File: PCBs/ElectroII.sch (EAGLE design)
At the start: 11 parts

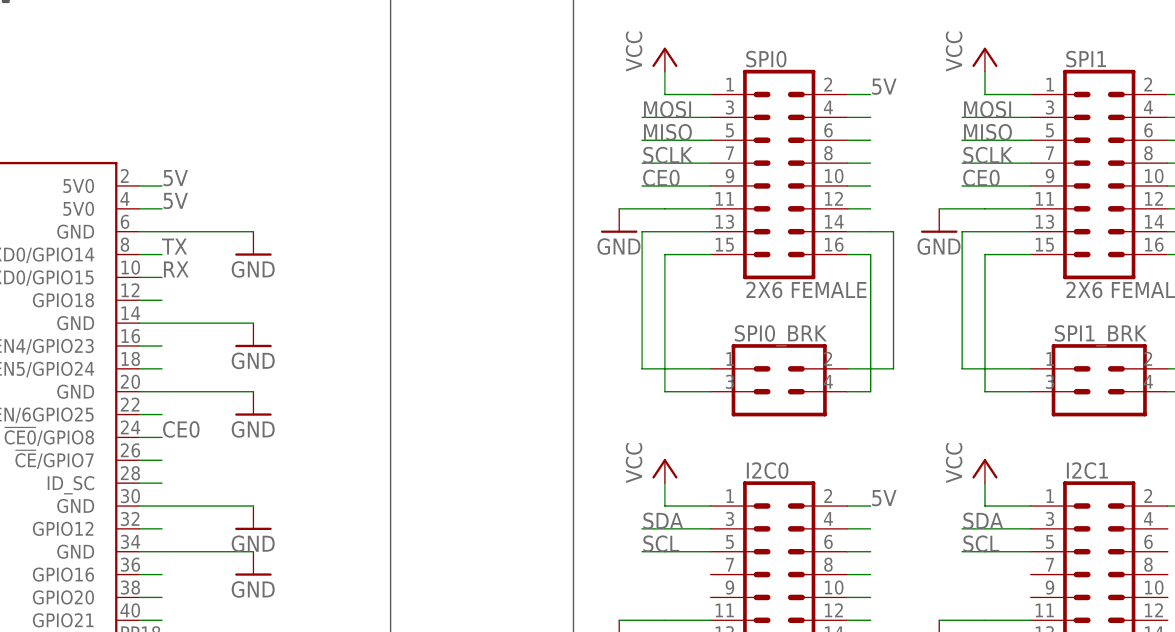
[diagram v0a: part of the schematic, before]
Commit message: Fixed a few mistakes in sensor breakouts
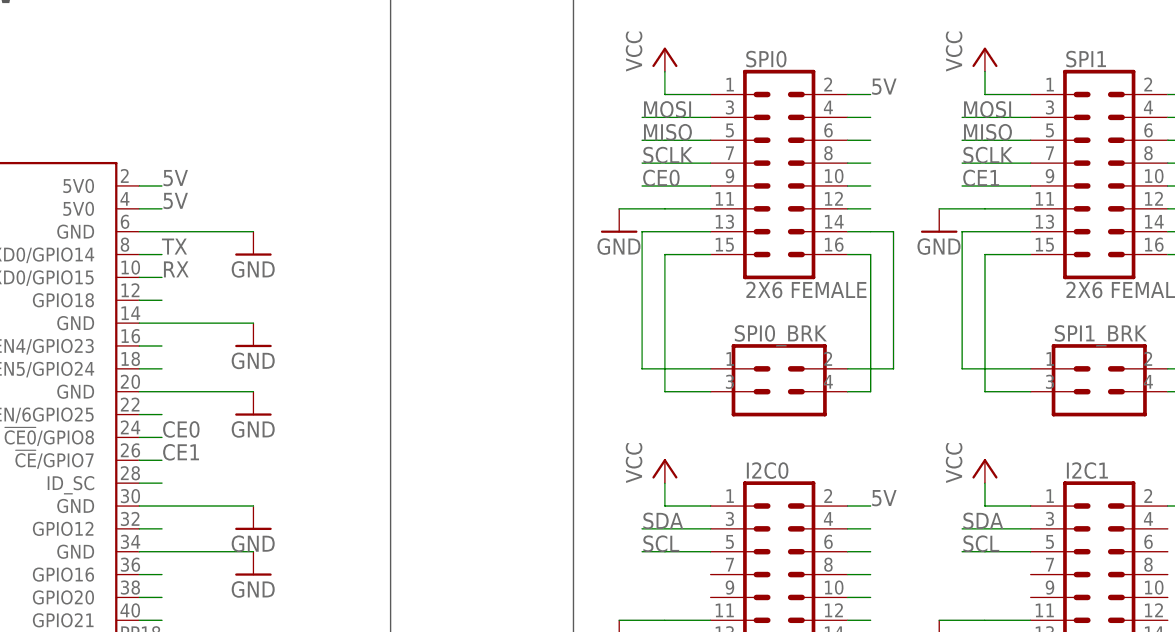
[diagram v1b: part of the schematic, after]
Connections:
- removed net N$8: U$1.!CE!/GPIO7
- new net CE1: SPI1.9, U$1.!CE!/GPIO7
- net CE0: no longer SPI1.9
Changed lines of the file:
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@@
 <label x="81.28" y="30.48" size="1.778" layer="95"/>
-</segment>
-<segment>
-<pinref part="SPI1" gate="G$1" pin="9"/>
-<wire x1="124.46" y1="30.48" x2="116.84" y2="30.48" width="0.1524" layer="91"/>
-<label x="116.84" y="30.48" size="1.778" layer="95"/>
-</segment>
-</net>
-<net name="N$8" class="0">
-<segment>
-<pinref part="U$1" gate="G$1" pin="!CE!/GPIO7"/>
-<wire x1="25.4" y1="0" x2="27.94" y2="0" width="0.1524" layer="91"/>
 </segment>
 </net>
@@
 </segment>
 </net>
+<net name="CE1" class="0">
+<segment>
+<pinref part="SPI1" gate="G$1" pin="9"/>
+<wire x1="124.46" y1="30.48" x2="116.84" y2="30.48" width="0.1524" layer="91"/>
+<label x="116.84" y="30.48" size="1.778" layer="95"/>
+</segment>
+<segment>
+<pinref part="U$1" gate="G$1" pin="!CE!/GPIO7"/>
+<wire x1="25.4" y1="0" x2="27.94" y2="0" width="0.1524" layer="91"/>
+<label x="27.94" y="0" size="1.778" layer="95"/>
+</segment>
+</net>

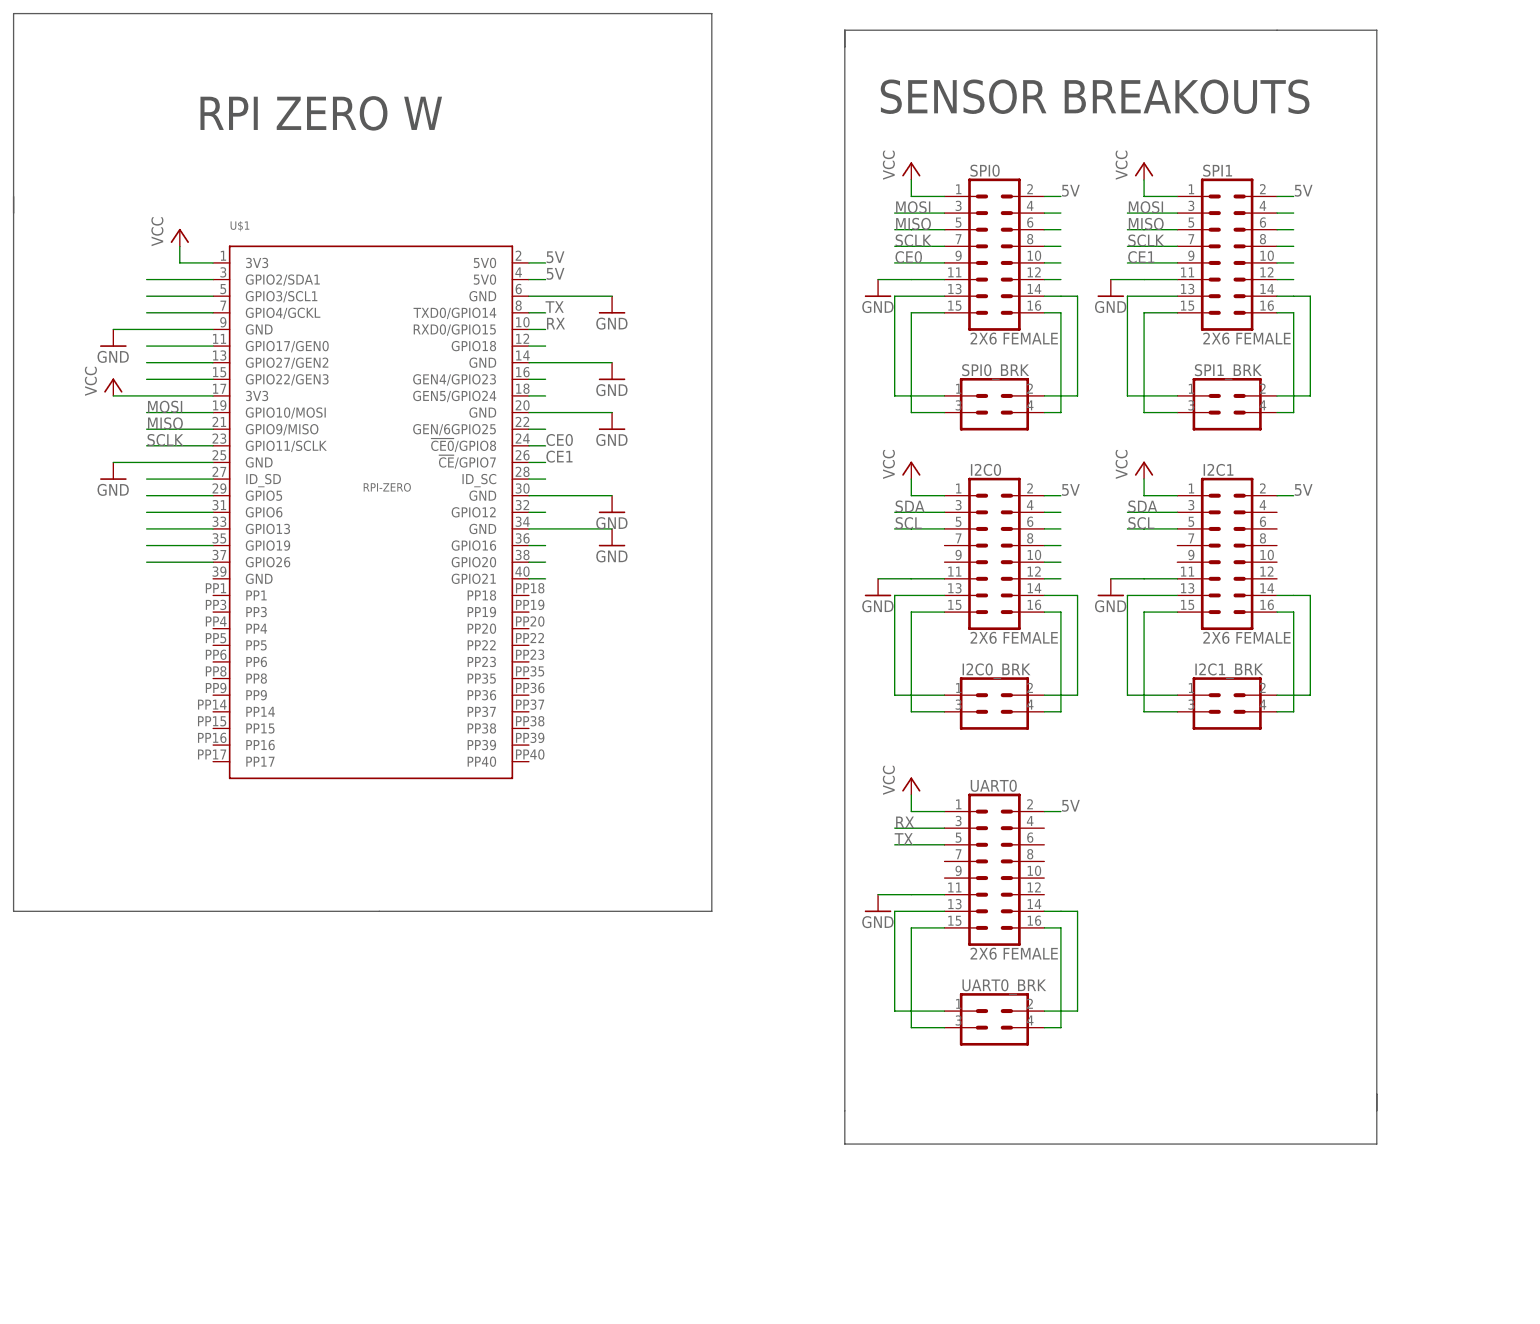
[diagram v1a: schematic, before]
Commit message: Transceiver added to Electro II
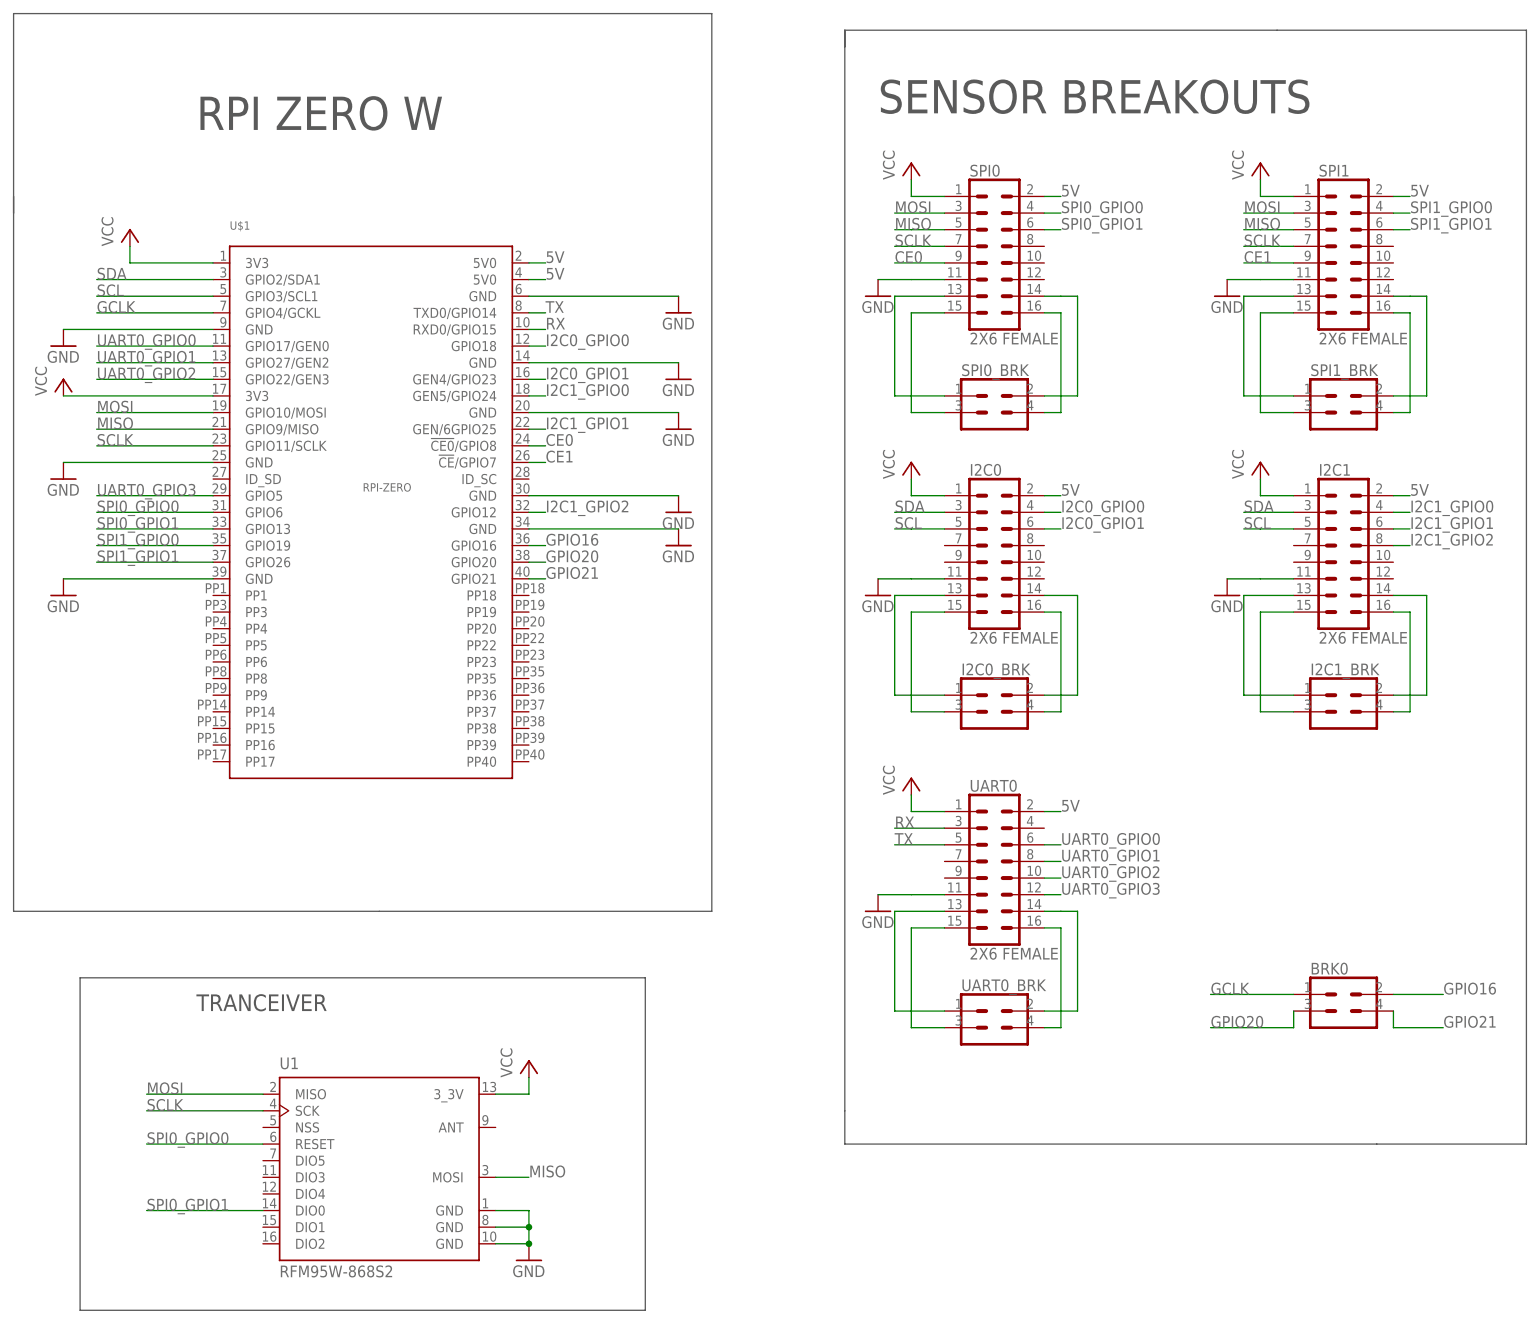
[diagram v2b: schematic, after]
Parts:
- added BRK0: SENSOR_PIN_BREAKOUT, RTR Main Library:SENSOR_PIN_BREAKOUT
- added U1: RFM95W-868S2, RTR Main Library:RFM95W-868S2
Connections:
- removed net N$10: U$1.GPIO12
- removed net N$11: U$1.GPIO16
- removed net N$12: U$1.GPIO20
- removed net N$13: U$1.GPIO21
- removed net N$16: SPI1.4
- removed net N$17: SPI1.6
- removed net N$18: SPI1.8
- removed net N$19: SPI1.10
- removed net N$21: SPI1.12
- removed net N$23: SPI0.4
- removed net N$24: SPI0.6
- removed net N$25: U$1.GPIO2/SDA1
- removed net N$26: U$1.GPIO3/SCL1
- removed net N$27: U$1.GPIO4/GCKL
- removed net N$28: U$1.GPIO17/GEN0
- removed net N$29: U$1.GPIO27/GEN2
- removed net N$3: U$1.GPIO18
- removed net N$30: U$1.GPIO22/GEN3
- removed net N$34: U$1.ID_SD
- removed net N$35: U$1.GPIO5
- removed net N$36: U$1.GPIO6
- removed net N$37: U$1.GPIO13
- removed net N$38: U$1.GPIO19
- removed net N$39: U$1.GPIO26
- removed net N$4: U$1.GEN4/GPIO23
- removed net N$40: SPI0.8
- removed net N$41: SPI0.10
- removed net N$42: SPI0.12
- removed net N$47: I2C0.4
- removed net N$48: I2C0.6
- removed net N$49: I2C0.8
- removed net N$5: U$1.GEN5/GPIO24
- removed net N$50: I2C0.10
- removed net N$51: I2C0.12
- removed net N$6: U$1.GEN/6GPIO25
- removed net N$9: U$1.ID_SC
- new net GCLK: BRK0.1, U$1.GPIO4/GCKL
- new net GPIO16: BRK0.2, U$1.GPIO16
- new net GPIO20: BRK0.3, U$1.GPIO20
- new net GPIO21: BRK0.4, U$1.GPIO21
- new net I2C0_GPIO0: I2C0.4, U$1.GPIO18
- new net I2C0_GPIO1: I2C0.6, U$1.GEN4/GPIO23
- new net I2C1_GPIO0: I2C1.4, U$1.GEN5/GPIO24
- new net I2C1_GPIO1: I2C1.6, U$1.GEN/6GPIO25
- new net I2C1_GPIO2: I2C1.8, U$1.GPIO12
- new net SPI0_GPIO0: SPI0.4, U$1.GPIO6, U1.RESET
- new net SPI0_GPIO1: SPI0.6, U$1.GPIO13, U1.DIO0
- new net SPI1_GPIO0: SPI1.4, U$1.GPIO19
- new net SPI1_GPIO1: SPI1.6, U$1.GPIO26
- new net UART0_GPIO0: U$1.GPIO17/GEN0, UART0.6
- new net UART0_GPIO1: U$1.GPIO27/GEN2, UART0.8
- new net UART0_GPIO2: U$1.GPIO22/GEN3, UART0.10
- new net UART0_GPIO3: U$1.GPIO5, UART0.12
- net GND: now also U$1.GND@3, U1.GND, U1.GND@1, U1.GND@2
- net MISO: now also U1.MOSI
- net MOSI: now also U1.MISO
- net SCL: now also U$1.GPIO3/SCL1
- net SCLK: now also U1.SCK
- net SDA: now also U$1.GPIO2/SDA1
- net VCC: now also U1.3_3V
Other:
- note added: "TRANCEIVER"
- moved on the sheet: I2C1, I2C1_BRK, SPI1, SPI1_BRK
